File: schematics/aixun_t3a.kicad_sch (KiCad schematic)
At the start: 90 parts, among them P3 Debug, P4 GX12-5, Q1 PNP, Q1 Q_NPN_BEC, Q3 AO4413, Q4 Q_NPN_BEC, SW1 SET, SW2 CH, U1 MY240H2416S-V2, U2 GD32F303RCT6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

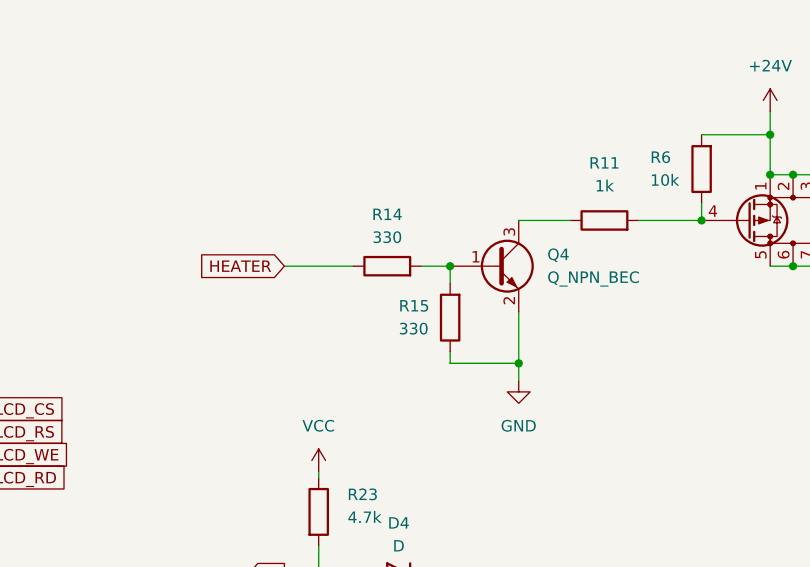
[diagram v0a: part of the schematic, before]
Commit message: schematics: fix values of R14, R15
Signed-off-by: Michael Niewöhner <foss@mniewoehner.de>
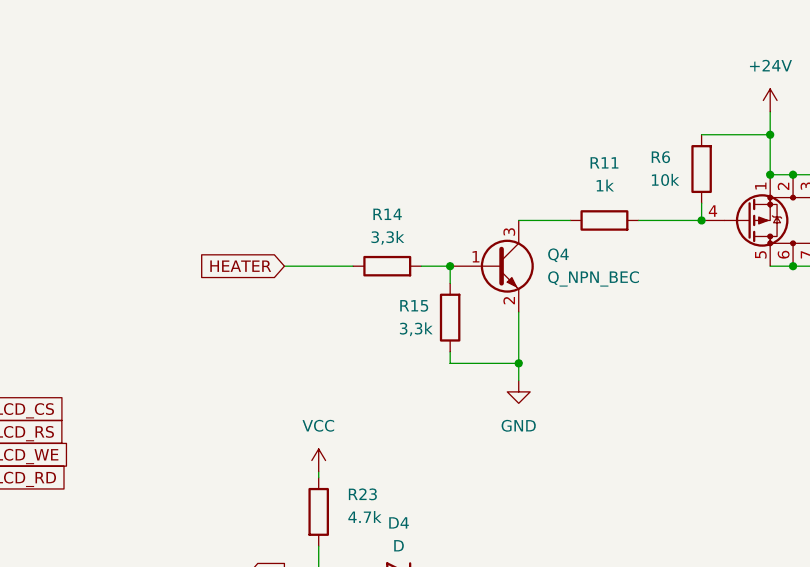
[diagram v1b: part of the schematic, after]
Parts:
- R14, R15: value 330 -> 3,3k
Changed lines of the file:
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@@
       (effects (font (size 1.27 1.27)) (justify right))
     )
-    (property "Value" "330" (at 313.055 117.475 0)
+    (property "Value" "3,3k" (at 313.055 117.475 0)
       (effects (font (size 1.27 1.27)) (justify right))
     )
@@
       (effects (font (size 1.27 1.27)))
     )
-    (property "Value" "330" (at 311.785 107.315 90)
-      (effects (font (size 1.27 1.27)))
-    )
+    (property "Value" "3,3k" (at 311.785 107.315 90)
+      (effects (font (size 1.27 1.27)))
+    )
